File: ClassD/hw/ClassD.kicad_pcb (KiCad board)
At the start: 2 copper layers, 81.2 x 56.9 mm, 66 parts, among them P1 RedRCA, P2 WhiteRCA, P3 CONN_01X02, P4 CONN_01X02, P5 CONN_01X02, SW1 SW_PUSH, SW2 SW_PUSH, U1 TDA7491LP, U2 MCP1700T

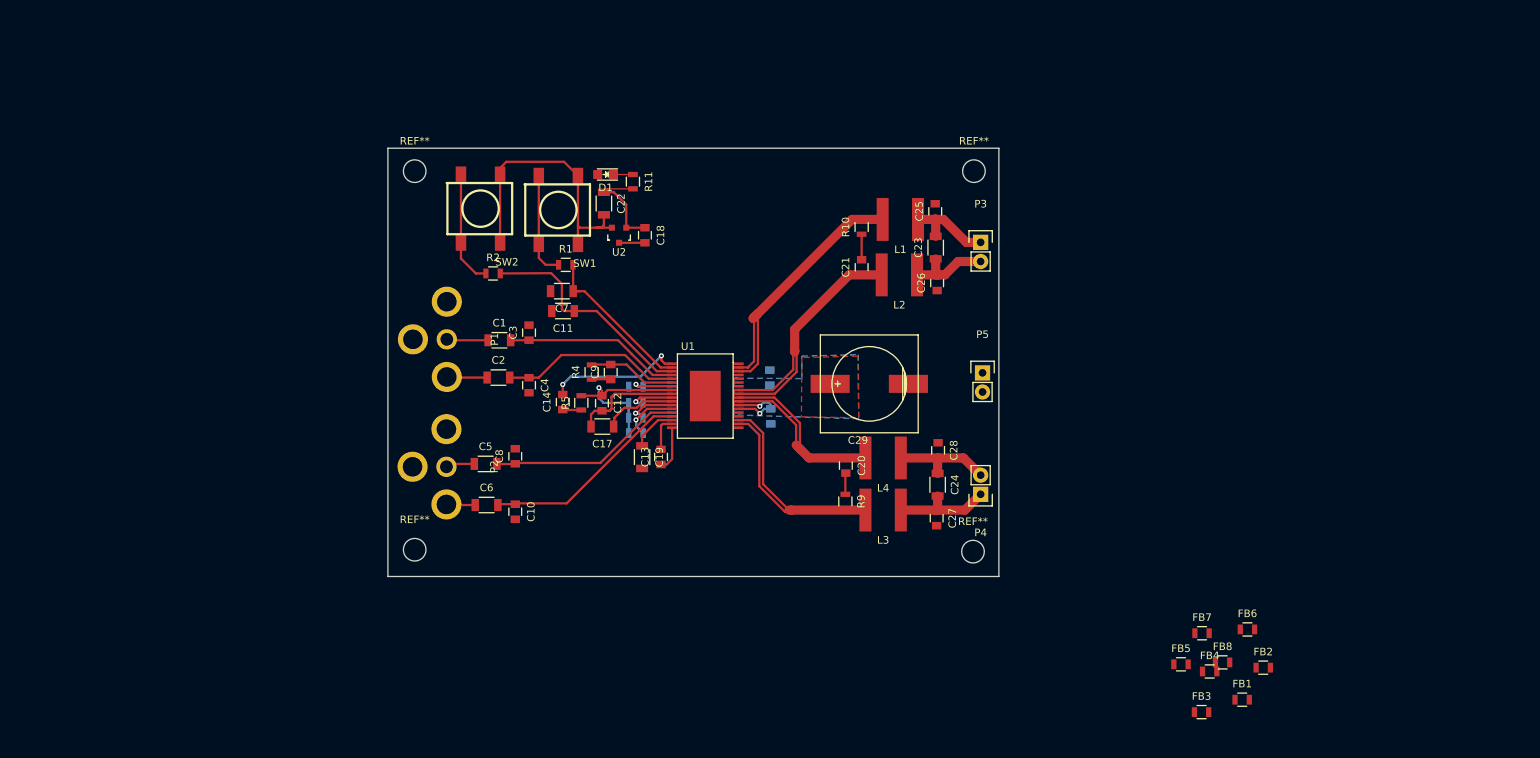
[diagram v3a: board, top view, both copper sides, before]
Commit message: Added planes and via stitching
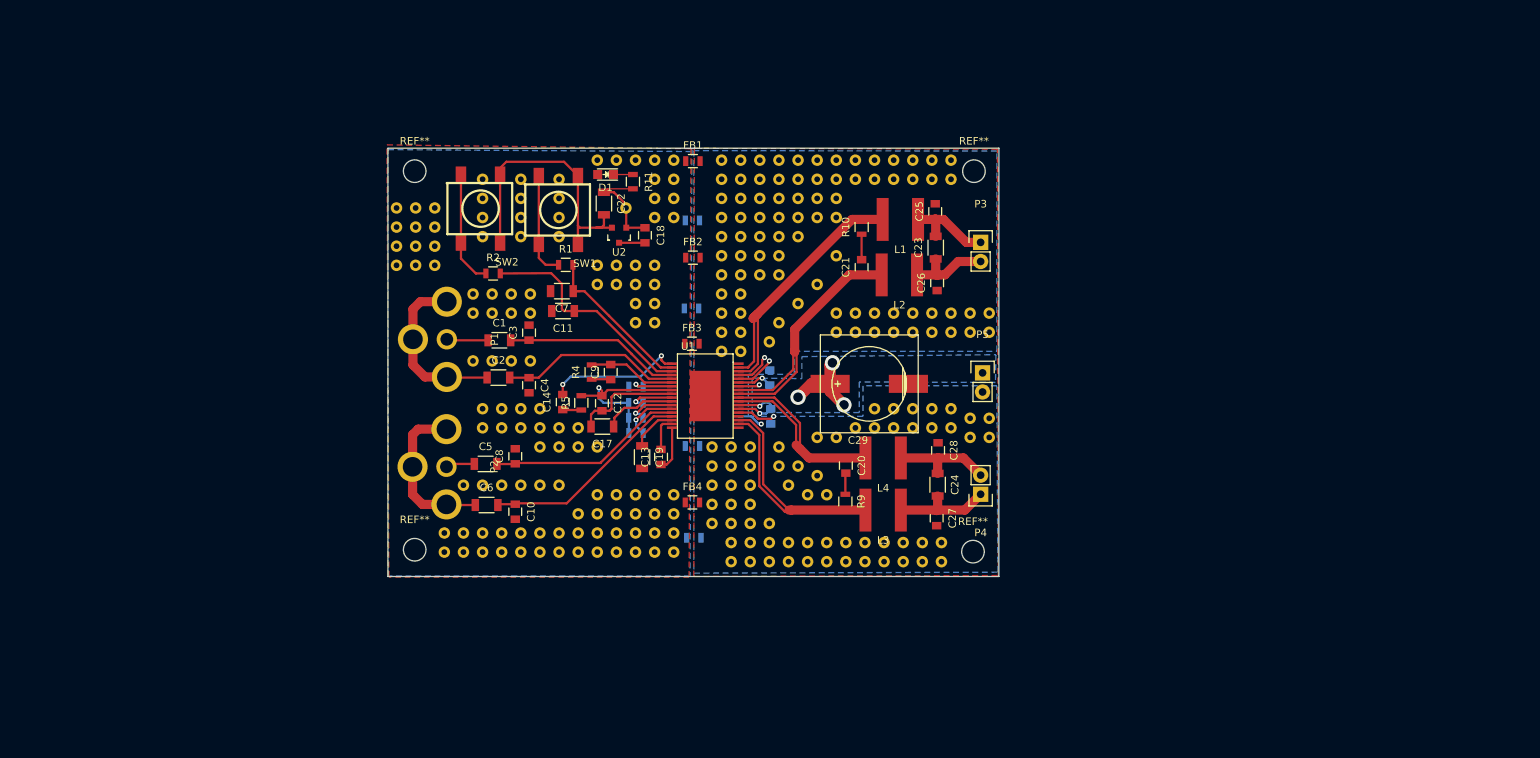
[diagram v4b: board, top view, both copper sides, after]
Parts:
- added REF**111111101: STITCH-VIA, ClassD:STITCH-VIA, F.Cu at (189.2, 88.9)
- added REF**111111102: STITCH-VIA, ClassD:STITCH-VIA, F.Cu at (189.2, 91.5)
- added REF**11111111: STITCH-VIA, ClassD:STITCH-VIA, F.Cu at (154.9, 110.5)
- added REF**11111111: STITCH-VIA, ClassD:STITCH-VIA, F.Cu at (149.8, 102.9)
- added REF**11111111: STITCH-VIA, ClassD:STITCH-VIA, F.Cu at (139.7, 94.0)
- added REF**11111111: STITCH-VIA, ClassD:STITCH-VIA, F.Cu at (139.7, 99.1)
- added REF**11111111: STITCH-VIA, ClassD:STITCH-VIA, F.Cu at (144.8, 96.5)
- added REF**11111111: STITCH-VIA, ClassD:STITCH-VIA, F.Cu at (144.8, 91.5)
- added REF**11111111: STITCH-VIA, ClassD:STITCH-VIA, F.Cu at (144.8, 94.0)
- added REF**11111111: STITCH-VIA, ClassD:STITCH-VIA, F.Cu at (144.8, 99.1)
- added REF**11111111: STITCH-VIA, ClassD:STITCH-VIA, F.Cu at (153.7, 95.3)
- added REF**11111111: STITCH-VIA, ClassD:STITCH-VIA, F.Cu at (157.5, 96.5)
- added REF**11111111: STITCH-VIA, ClassD:STITCH-VIA, F.Cu at (160.0, 96.5)
- added REF**11111111: STITCH-VIA, ClassD:STITCH-VIA, F.Cu at (157.5, 94.0)
- added REF**11111111: STITCH-VIA, ClassD:STITCH-VIA, F.Cu at (157.5, 105.4)
- added REF**11111111: STITCH-VIA, ClassD:STITCH-VIA, F.Cu at (160.0, 94.0)
- added REF**11111111: STITCH-VIA, ClassD:STITCH-VIA, F.Cu at (157.5, 91.5)
- added REF**11111111: STITCH-VIA, ClassD:STITCH-VIA, F.Cu at (160.0, 91.5)
- added REF**11111111: STITCH-VIA, ClassD:STITCH-VIA, F.Cu at (149.8, 88.9)
- added REF**11111111: STITCH-VIA, ClassD:STITCH-VIA, F.Cu at (152.4, 88.9)
- added REF**11111111: STITCH-VIA, ClassD:STITCH-VIA, F.Cu at (154.9, 88.9)
- added REF**11111111: STITCH-VIA, ClassD:STITCH-VIA, F.Cu at (157.5, 88.9)
- added REF**11111111: STITCH-VIA, ClassD:STITCH-VIA, F.Cu at (160.0, 88.9)
- added REF**11111111: STITCH-VIA, ClassD:STITCH-VIA, F.Cu at (166.4, 99.1)
- added REF**11111111: STITCH-VIA, ClassD:STITCH-VIA, F.Cu at (166.4, 88.9)
- added REF**11111111: STITCH-VIA, ClassD:STITCH-VIA, F.Cu at (157.5, 102.9)
- added REF**11111111: STITCH-VIA, ClassD:STITCH-VIA, F.Cu at (147.3, 124.5)
- added REF**11111111: STITCH-VIA, ClassD:STITCH-VIA, F.Cu at (144.8, 124.5)
- added REF**11111111: STITCH-VIA, ClassD:STITCH-VIA, F.Cu at (149.8, 127.0)
- added REF**11111111: STITCH-VIA, ClassD:STITCH-VIA, F.Cu at (147.3, 127.0)
- added REF**11111111: STITCH-VIA, ClassD:STITCH-VIA, F.Cu at (144.8, 127.0)
- added REF**11111111: STITCH-VIA, ClassD:STITCH-VIA, F.Cu at (142.2, 127.0)
- added REF**11111111: STITCH-VIA, ClassD:STITCH-VIA, F.Cu at (160.0, 141.0)
- added REF**11111111: STITCH-VIA, ClassD:STITCH-VIA, F.Cu at (157.5, 110.5)
- added REF**11111111: STITCH-VIA, ClassD:STITCH-VIA, F.Cu at (160.0, 138.4)
- added REF**11111111: STITCH-VIA, ClassD:STITCH-VIA, F.Cu at (160.0, 133.4)
- added REF**11111111: STITCH-VIA, ClassD:STITCH-VIA, F.Cu at (157.5, 133.4)
- added REF**11111111: STITCH-VIA, ClassD:STITCH-VIA, F.Cu at (154.9, 133.4)
- added REF**11111111: STITCH-VIA, ClassD:STITCH-VIA, F.Cu at (149.8, 133.4)
- added REF**11111111: STITCH-VIA, ClassD:STITCH-VIA, F.Cu at (152.4, 133.4)
- added REF**11111111: STITCH-VIA, ClassD:STITCH-VIA, F.Cu at (157.5, 135.9)
- added REF**11111111: STITCH-VIA, ClassD:STITCH-VIA, F.Cu at (154.9, 135.9)
- added REF**11111111: STITCH-VIA, ClassD:STITCH-VIA, F.Cu at (149.8, 135.9)
- added REF**11111111: STITCH-VIA, ClassD:STITCH-VIA, F.Cu at (152.4, 135.9)
- added REF**11111111: STITCH-VIA, ClassD:STITCH-VIA, F.Cu at (154.9, 108.0)
- added REF**11111111: STITCH-VIA, ClassD:STITCH-VIA, F.Cu at (160.0, 135.9)
- added REF**11111111: STITCH-VIA, ClassD:STITCH-VIA, F.Cu at (147.3, 135.9)
- added REF**11111111: STITCH-VIA, ClassD:STITCH-VIA, F.Cu at (154.9, 138.4)
- added REF**11111111: STITCH-VIA, ClassD:STITCH-VIA, F.Cu at (152.4, 138.4)
- added REF**11111111: STITCH-VIA, ClassD:STITCH-VIA, F.Cu at (147.3, 138.4)
- added REF**11111111: STITCH-VIA, ClassD:STITCH-VIA, F.Cu at (149.8, 138.4)
- added REF**11111111: STITCH-VIA, ClassD:STITCH-VIA, F.Cu at (157.5, 138.4)
- added REF**11111111: STITCH-VIA, ClassD:STITCH-VIA, F.Cu at (144.8, 138.4)
- added REF**11111111: STITCH-VIA, ClassD:STITCH-VIA, F.Cu at (154.9, 141.0)
- added REF**11111111: STITCH-VIA, ClassD:STITCH-VIA, F.Cu at (152.4, 141.0)
- added REF**11111111: STITCH-VIA, ClassD:STITCH-VIA, F.Cu at (157.5, 108.0)
- added REF**11111111: STITCH-VIA, ClassD:STITCH-VIA, F.Cu at (147.3, 141.0)
- added REF**11111111: STITCH-VIA, ClassD:STITCH-VIA, F.Cu at (149.8, 141.0)
- added REF**11111111: STITCH-VIA, ClassD:STITCH-VIA, F.Cu at (157.5, 141.0)
- added REF**11111111: STITCH-VIA, ClassD:STITCH-VIA, F.Cu at (144.8, 141.0)
- added REF**11111111: STITCH-VIA, ClassD:STITCH-VIA, F.Cu at (139.7, 141.0)
- added REF**11111111: STITCH-VIA, ClassD:STITCH-VIA, F.Cu at (137.1, 141.0)
- added REF**11111111: STITCH-VIA, ClassD:STITCH-VIA, F.Cu at (132.1, 141.0)
- added REF**11111111: STITCH-VIA, ClassD:STITCH-VIA, F.Cu at (134.6, 141.0)
- added REF**11111111: STITCH-VIA, ClassD:STITCH-VIA, F.Cu at (142.2, 141.0)
- added REF**11111111: STITCH-VIA, ClassD:STITCH-VIA, F.Cu at (129.5, 141.0)
- added REF**11111111: STITCH-VIA, ClassD:STITCH-VIA, F.Cu at (154.9, 102.9)
- added REF**11111111: STITCH-VIA, ClassD:STITCH-VIA, F.Cu at (139.7, 138.4)
- added REF**11111111: STITCH-VIA, ClassD:STITCH-VIA, F.Cu at (137.1, 138.4)
- added REF**11111111: STITCH-VIA, ClassD:STITCH-VIA, F.Cu at (132.1, 138.4)
- added REF**11111111: STITCH-VIA, ClassD:STITCH-VIA, F.Cu at (134.6, 138.4)
- added REF**11111111: STITCH-VIA, ClassD:STITCH-VIA, F.Cu at (142.2, 138.4)
- added REF**11111111: STITCH-VIA, ClassD:STITCH-VIA, F.Cu at (129.5, 138.4)
- added REF**11111111: STITCH-VIA, ClassD:STITCH-VIA, F.Cu at (142.2, 132.1)
- added REF**11111111: STITCH-VIA, ClassD:STITCH-VIA, F.Cu at (144.8, 132.1)
- added REF**11111111: STITCH-VIA, ClassD:STITCH-VIA, F.Cu at (132.1, 132.1)
- added REF**11111111: STITCH-VIA, ClassD:STITCH-VIA, F.Cu at (134.6, 132.1)
- added REF**11111111: STITCH-VIA, ClassD:STITCH-VIA, F.Cu at (152.4, 105.4)
- added REF**11111111: STITCH-VIA, ClassD:STITCH-VIA, F.Cu at (137.1, 132.1)
- added REF**11111111: STITCH-VIA, ClassD:STITCH-VIA, F.Cu at (139.7, 132.1)
- added REF**11111111: STITCH-VIA, ClassD:STITCH-VIA, F.Cu at (134.6, 124.5)
- added REF**11111111: STITCH-VIA, ClassD:STITCH-VIA, F.Cu at (137.1, 124.5)
- added REF**11111111: STITCH-VIA, ClassD:STITCH-VIA, F.Cu at (139.7, 124.5)
- added REF**11111111: STITCH-VIA, ClassD:STITCH-VIA, F.Cu at (142.2, 124.5)
- added REF**11111111: STITCH-VIA, ClassD:STITCH-VIA, F.Cu at (134.6, 121.9)
- added REF**11111111: STITCH-VIA, ClassD:STITCH-VIA, F.Cu at (137.1, 121.9)
- added REF**11111111: STITCH-VIA, ClassD:STITCH-VIA, F.Cu at (139.7, 121.9)
- added REF**11111111: STITCH-VIA, ClassD:STITCH-VIA, F.Cu at (142.2, 121.9)
- added REF**11111111: STITCH-VIA, ClassD:STITCH-VIA, F.Cu at (154.9, 105.4)
- added REF**11111111: STITCH-VIA, ClassD:STITCH-VIA, F.Cu at (133.3, 115.6)
- added REF**11111111: STITCH-VIA, ClassD:STITCH-VIA, F.Cu at (135.9, 115.6)
- added REF**11111111: STITCH-VIA, ClassD:STITCH-VIA, F.Cu at (138.4, 115.6)
- added REF**11111111: STITCH-VIA, ClassD:STITCH-VIA, F.Cu at (141.0, 115.6)
- added REF**11111111: STITCH-VIA, ClassD:STITCH-VIA, F.Cu at (133.3, 109.2)
- added REF**11111111: STITCH-VIA, ClassD:STITCH-VIA, F.Cu at (135.9, 109.2)
- added REF**11111111: STITCH-VIA, ClassD:STITCH-VIA, F.Cu at (138.4, 109.2)
- added REF**11111111: STITCH-VIA, ClassD:STITCH-VIA, F.Cu at (141.0, 109.2)
- added REF**11111111: STITCH-VIA, ClassD:STITCH-VIA, F.Cu at (141.0, 106.7)
- added REF**11111111: STITCH-VIA, ClassD:STITCH-VIA, F.Cu at (138.4, 106.7)
- added REF**11111111: STITCH-VIA, ClassD:STITCH-VIA, F.Cu at (149.8, 105.4)
- added REF**11111111: STITCH-VIA, ClassD:STITCH-VIA, F.Cu at (133.3, 106.7)
- added REF**11111111: STITCH-VIA, ClassD:STITCH-VIA, F.Cu at (135.9, 106.7)
- added REF**11111111: STITCH-VIA, ClassD:STITCH-VIA, F.Cu at (128.3, 100.3)
- added REF**11111111: STITCH-VIA, ClassD:STITCH-VIA, F.Cu at (128.3, 95.3)
- added REF**11111111: STITCH-VIA, ClassD:STITCH-VIA, F.Cu at (128.3, 97.8)
- added REF**11111111: STITCH-VIA, ClassD:STITCH-VIA, F.Cu at (128.3, 102.9)
- added REF**11111111: STITCH-VIA, ClassD:STITCH-VIA, F.Cu at (125.7, 100.3)
- added REF**11111111: STITCH-VIA, ClassD:STITCH-VIA, F.Cu at (125.7, 95.3)
- added REF**11111111: STITCH-VIA, ClassD:STITCH-VIA, F.Cu at (125.7, 97.8)
- added REF**11111111: STITCH-VIA, ClassD:STITCH-VIA, F.Cu at (125.7, 102.9)
- added REF**11111111: STITCH-VIA, ClassD:STITCH-VIA, F.Cu at (152.4, 102.9)
- added REF**11111111: STITCH-VIA, ClassD:STITCH-VIA, F.Cu at (123.2, 100.3)
- added REF**11111111: STITCH-VIA, ClassD:STITCH-VIA, F.Cu at (123.2, 95.3)
- added REF**11111111: STITCH-VIA, ClassD:STITCH-VIA, F.Cu at (123.2, 97.8)
- added REF**11111111: STITCH-VIA, ClassD:STITCH-VIA, F.Cu at (123.2, 102.9)
- added REF**11111111: STITCH-VIA, ClassD:STITCH-VIA, F.Cu at (134.6, 96.5)
- added REF**11111111: STITCH-VIA, ClassD:STITCH-VIA, F.Cu at (134.6, 91.5)
- added REF**11111111: STITCH-VIA, ClassD:STITCH-VIA, F.Cu at (134.6, 94.0)
- added REF**11111111: STITCH-VIA, ClassD:STITCH-VIA, F.Cu at (134.6, 99.1)
- added REF**11111111: STITCH-VIA, ClassD:STITCH-VIA, F.Cu at (139.7, 96.5)
- added REF**11111111: STITCH-VIA, ClassD:STITCH-VIA, F.Cu at (139.7, 91.5)
- added REF**111111111: STITCH-VIA, ClassD:STITCH-VIA, F.Cu at (196.8, 111.8)
- added REF**111111111: STITCH-VIA, ClassD:STITCH-VIA, F.Cu at (191.8, 111.8)
- added REF**111111111: STITCH-VIA, ClassD:STITCH-VIA, F.Cu at (186.7, 111.8)
- added REF**111111111: STITCH-VIA, ClassD:STITCH-VIA, F.Cu at (181.6, 111.8)
- added REF**111111111: STITCH-VIA, ClassD:STITCH-VIA, F.Cu at (166.4, 114.3)
- added REF**111111111: STITCH-VIA, ClassD:STITCH-VIA, F.Cu at (166.4, 109.2)
- added REF**111111111: STITCH-VIA, ClassD:STITCH-VIA, F.Cu at (166.4, 104.2)
- added REF**111111111: STITCH-VIA, ClassD:STITCH-VIA, F.Cu at (166.4, 94.0)
- added REF**111111111: STITCH-VIA, ClassD:STITCH-VIA, F.Cu at (191.8, 88.9)
- added REF**111111112: STITCH-VIA, ClassD:STITCH-VIA, F.Cu at (166.4, 96.5)
- added REF**111111112: STITCH-VIA, ClassD:STITCH-VIA, F.Cu at (191.8, 91.5)
- added REF**11111112: STITCH-VIA, ClassD:STITCH-VIA, F.Cu at (196.8, 109.2)
- added REF**11111112: STITCH-VIA, ClassD:STITCH-VIA, F.Cu at (191.8, 109.2)
- added REF**11111112: STITCH-VIA, ClassD:STITCH-VIA, F.Cu at (186.7, 109.2)
- added REF**11111112: STITCH-VIA, ClassD:STITCH-VIA, F.Cu at (181.6, 109.2)
- added REF**11111112: STITCH-VIA, ClassD:STITCH-VIA, F.Cu at (166.4, 111.8)
- added REF**11111112: STITCH-VIA, ClassD:STITCH-VIA, F.Cu at (166.4, 106.7)
- added REF**11111112: STITCH-VIA, ClassD:STITCH-VIA, F.Cu at (166.4, 101.6)
- added REF**11111112: STITCH-VIA, ClassD:STITCH-VIA, F.Cu at (166.4, 91.5)
- added REF**111111121: STITCH-VIA, ClassD:STITCH-VIA, F.Cu at (170.2, 142.3)
- added REF**111111121: STITCH-VIA, ClassD:STITCH-VIA, F.Cu at (193.0, 142.3)
- added REF**111111121: STITCH-VIA, ClassD:STITCH-VIA, F.Cu at (195.6, 142.3)
- added REF**111111121: STITCH-VIA, ClassD:STITCH-VIA, F.Cu at (187.9, 142.3)
- added REF**111111121: STITCH-VIA, ClassD:STITCH-VIA, F.Cu at (181.6, 101.6)
- added REF**111111121: STITCH-VIA, ClassD:STITCH-VIA, F.Cu at (179.1, 105.4)
- added REF**111111121: STITCH-VIA, ClassD:STITCH-VIA, F.Cu at (176.5, 108.0)
- added REF**111111121: STITCH-VIA, ClassD:STITCH-VIA, F.Cu at (174.0, 110.5)
- added REF**111111121: STITCH-VIA, ClassD:STITCH-VIA, F.Cu at (172.7, 113.0)
- added REF**111111121: STITCH-VIA, ClassD:STITCH-VIA, F.Cu at (179.1, 125.7)
- added REF**111111121: STITCH-VIA, ClassD:STITCH-VIA, F.Cu at (181.6, 125.7)
- added REF**111111121: STITCH-VIA, ClassD:STITCH-VIA, F.Cu at (172.7, 142.3)
- added REF**111111121: STITCH-VIA, ClassD:STITCH-VIA, F.Cu at (176.5, 129.6)
- added REF**111111121: STITCH-VIA, ClassD:STITCH-VIA, F.Cu at (177.8, 133.4)
- added REF**111111121: STITCH-VIA, ClassD:STITCH-VIA, F.Cu at (180.3, 133.4)
- added REF**111111121: STITCH-VIA, ClassD:STITCH-VIA, F.Cu at (179.1, 130.8)
- added REF**111111121: STITCH-VIA, ClassD:STITCH-VIA, F.Cu at (175.2, 132.1)
- added REF**111111121: STITCH-VIA, ClassD:STITCH-VIA, F.Cu at (174.0, 129.6)
- added REF**111111121: STITCH-VIA, ClassD:STITCH-VIA, F.Cu at (174.0, 127.0)
- added REF**111111121: STITCH-VIA, ClassD:STITCH-VIA, F.Cu at (184.1, 124.5)
- added REF**111111121: STITCH-VIA, ClassD:STITCH-VIA, F.Cu at (186.7, 124.5)
- added REF**111111121: STITCH-VIA, ClassD:STITCH-VIA, F.Cu at (189.2, 124.5)
- added REF**111111121: STITCH-VIA, ClassD:STITCH-VIA, F.Cu at (175.2, 142.3)
- added REF**111111121: STITCH-VIA, ClassD:STITCH-VIA, F.Cu at (191.8, 124.5)
- added REF**111111121: STITCH-VIA, ClassD:STITCH-VIA, F.Cu at (194.3, 124.5)
- added REF**111111121: STITCH-VIA, ClassD:STITCH-VIA, F.Cu at (196.8, 124.5)
- added REF**111111121: STITCH-VIA, ClassD:STITCH-VIA, F.Cu at (199.4, 125.7)
- added REF**111111121: STITCH-VIA, ClassD:STITCH-VIA, F.Cu at (201.9, 125.7)
- added REF**111111121: STITCH-VIA, ClassD:STITCH-VIA, F.Cu at (201.9, 111.8)
- added REF**111111121: STITCH-VIA, ClassD:STITCH-VIA, F.Cu at (199.4, 111.8)
- added REF**111111121: STITCH-VIA, ClassD:STITCH-VIA, F.Cu at (194.3, 111.8)
- added REF**111111121: STITCH-VIA, ClassD:STITCH-VIA, F.Cu at (189.2, 111.8)
- added REF**111111121: STITCH-VIA, ClassD:STITCH-VIA, F.Cu at (184.1, 111.8)
- added REF**111111121: STITCH-VIA, ClassD:STITCH-VIA, F.Cu at (167.6, 142.3)
- added REF**111111121: STITCH-VIA, ClassD:STITCH-VIA, F.Cu at (168.9, 114.3)
- added REF**111111121: STITCH-VIA, ClassD:STITCH-VIA, F.Cu at (168.9, 109.2)
- added REF**111111121: STITCH-VIA, ClassD:STITCH-VIA, F.Cu at (168.9, 104.2)
- added REF**111111121: STITCH-VIA, ClassD:STITCH-VIA, F.Cu at (168.9, 94.0)
- added REF**111111121: STITCH-VIA, ClassD:STITCH-VIA, F.Cu at (194.3, 88.9)
- added REF**111111121: STITCH-VIA, ClassD:STITCH-VIA, F.Cu at (180.3, 142.3)
- added REF**111111121: STITCH-VIA, ClassD:STITCH-VIA, F.Cu at (182.9, 142.3)
- added REF**111111121: STITCH-VIA, ClassD:STITCH-VIA, F.Cu at (185.4, 142.3)
- added REF**111111121: STITCH-VIA, ClassD:STITCH-VIA, F.Cu at (177.8, 142.3)
- added REF**111111121: STITCH-VIA, ClassD:STITCH-VIA, F.Cu at (190.5, 142.3)
- added REF**111111122: STITCH-VIA, ClassD:STITCH-VIA, F.Cu at (168.9, 96.5)
- added REF**111111122: STITCH-VIA, ClassD:STITCH-VIA, F.Cu at (194.3, 91.5)
- added REF**111111131: STITCH-VIA, ClassD:STITCH-VIA, F.Cu at (171.4, 104.2)
- added REF**111111131: STITCH-VIA, ClassD:STITCH-VIA, F.Cu at (171.4, 94.0)
- added REF**111111131: STITCH-VIA, ClassD:STITCH-VIA, F.Cu at (196.8, 88.9)
- added REF**111111132: STITCH-VIA, ClassD:STITCH-VIA, F.Cu at (171.4, 96.5)
- added REF**111111132: STITCH-VIA, ClassD:STITCH-VIA, F.Cu at (196.8, 91.5)
- added REF**111111141: STITCH-VIA, ClassD:STITCH-VIA, F.Cu at (174.0, 104.2)
- added REF**111111141: STITCH-VIA, ClassD:STITCH-VIA, F.Cu at (174.0, 94.0)
- added REF**111111142: STITCH-VIA, ClassD:STITCH-VIA, F.Cu at (174.0, 96.5)
- added REF**111111151: STITCH-VIA, ClassD:STITCH-VIA, F.Cu at (176.5, 94.0)
- added REF**111111152: STITCH-VIA, ClassD:STITCH-VIA, F.Cu at (176.5, 99.1)
- added REF**111111152: STITCH-VIA, ClassD:STITCH-VIA, F.Cu at (176.5, 96.5)
- added REF**111111161: STITCH-VIA, ClassD:STITCH-VIA, F.Cu at (179.1, 94.0)
- added REF**111111162: STITCH-VIA, ClassD:STITCH-VIA, F.Cu at (179.1, 96.5)
- added REF**111111171: STITCH-VIA, ClassD:STITCH-VIA, F.Cu at (181.6, 94.0)
- added REF**111111172: STITCH-VIA, ClassD:STITCH-VIA, F.Cu at (181.6, 96.5)
- added REF**11111121: STITCH-VIA, ClassD:STITCH-VIA, F.Cu at (168.9, 99.1)
- added REF**11111121: STITCH-VIA, ClassD:STITCH-VIA, F.Cu at (168.9, 88.9)
- added REF**11111122: STITCH-VIA, ClassD:STITCH-VIA, F.Cu at (170.2, 127.0)
- added REF**11111122: STITCH-VIA, ClassD:STITCH-VIA, F.Cu at (170.2, 134.6)
- added REF**11111122: STITCH-VIA, ClassD:STITCH-VIA, F.Cu at (165.1, 134.6)
- added REF**11111122: STITCH-VIA, ClassD:STITCH-VIA, F.Cu at (167.6, 134.6)
- added REF**11111122: STITCH-VIA, ClassD:STITCH-VIA, F.Cu at (172.7, 137.2)
- added REF**11111122: STITCH-VIA, ClassD:STITCH-VIA, F.Cu at (170.2, 137.2)
- added REF**11111122: STITCH-VIA, ClassD:STITCH-VIA, F.Cu at (165.1, 137.2)
- added REF**11111122: STITCH-VIA, ClassD:STITCH-VIA, F.Cu at (167.6, 137.2)
- added REF**11111122: STITCH-VIA, ClassD:STITCH-VIA, F.Cu at (170.2, 139.7)
- added REF**11111122: STITCH-VIA, ClassD:STITCH-VIA, F.Cu at (167.6, 139.7)
- added REF**11111122: STITCH-VIA, ClassD:STITCH-VIA, F.Cu at (172.7, 139.7)
- added REF**11111122: STITCH-VIA, ClassD:STITCH-VIA, F.Cu at (167.6, 127.0)
- added REF**11111122: STITCH-VIA, ClassD:STITCH-VIA, F.Cu at (175.2, 139.7)
- added REF**11111122: STITCH-VIA, ClassD:STITCH-VIA, F.Cu at (180.3, 139.7)
- added REF**11111122: STITCH-VIA, ClassD:STITCH-VIA, F.Cu at (177.8, 139.7)
- added REF**11111122: STITCH-VIA, ClassD:STITCH-VIA, F.Cu at (182.9, 139.7)
- added REF**11111122: STITCH-VIA, ClassD:STITCH-VIA, F.Cu at (185.4, 139.7)
- added REF**11111122: STITCH-VIA, ClassD:STITCH-VIA, F.Cu at (190.5, 139.7)
- added REF**11111122: STITCH-VIA, ClassD:STITCH-VIA, F.Cu at (187.9, 139.7)
- added REF**11111122: STITCH-VIA, ClassD:STITCH-VIA, F.Cu at (193.0, 139.7)
- added REF**11111122: STITCH-VIA, ClassD:STITCH-VIA, F.Cu at (195.6, 139.7)
- added REF**11111122: STITCH-VIA, ClassD:STITCH-VIA, F.Cu at (186.7, 121.9)
- added REF**11111122: STITCH-VIA, ClassD:STITCH-VIA, F.Cu at (165.1, 127.0)
- added REF**11111122: STITCH-VIA, ClassD:STITCH-VIA, F.Cu at (189.2, 121.9)
- added REF**11111122: STITCH-VIA, ClassD:STITCH-VIA, F.Cu at (191.8, 121.9)
- added REF**11111122: STITCH-VIA, ClassD:STITCH-VIA, F.Cu at (194.3, 121.9)
- added REF**11111122: STITCH-VIA, ClassD:STITCH-VIA, F.Cu at (196.8, 121.9)
- added REF**11111122: STITCH-VIA, ClassD:STITCH-VIA, F.Cu at (199.4, 123.2)
- added REF**11111122: STITCH-VIA, ClassD:STITCH-VIA, F.Cu at (201.9, 123.2)
- added REF**11111122: STITCH-VIA, ClassD:STITCH-VIA, F.Cu at (201.9, 109.2)
- added REF**11111122: STITCH-VIA, ClassD:STITCH-VIA, F.Cu at (199.4, 109.2)
- added REF**11111122: STITCH-VIA, ClassD:STITCH-VIA, F.Cu at (194.3, 109.2)
- added REF**11111122: STITCH-VIA, ClassD:STITCH-VIA, F.Cu at (189.2, 109.2)
- added REF**11111122: STITCH-VIA, ClassD:STITCH-VIA, F.Cu at (170.2, 129.6)
- added REF**11111122: STITCH-VIA, ClassD:STITCH-VIA, F.Cu at (184.1, 109.2)
- added REF**11111122: STITCH-VIA, ClassD:STITCH-VIA, F.Cu at (168.9, 111.8)
- added REF**11111122: STITCH-VIA, ClassD:STITCH-VIA, F.Cu at (168.9, 106.7)
- added REF**11111122: STITCH-VIA, ClassD:STITCH-VIA, F.Cu at (168.9, 101.6)
- added REF**11111122: STITCH-VIA, ClassD:STITCH-VIA, F.Cu at (168.9, 91.5)
- added REF**11111122: STITCH-VIA, ClassD:STITCH-VIA, F.Cu at (165.1, 129.6)
- added REF**11111122: STITCH-VIA, ClassD:STITCH-VIA, F.Cu at (167.6, 129.6)
- added REF**11111122: STITCH-VIA, ClassD:STITCH-VIA, F.Cu at (170.2, 132.1)
- added REF**11111122: STITCH-VIA, ClassD:STITCH-VIA, F.Cu at (165.1, 132.1)
- added REF**11111122: STITCH-VIA, ClassD:STITCH-VIA, F.Cu at (167.6, 132.1)
- added REF**11111131: STITCH-VIA, ClassD:STITCH-VIA, F.Cu at (171.4, 99.1)
- added REF**11111131: STITCH-VIA, ClassD:STITCH-VIA, F.Cu at (171.4, 88.9)
- added REF**11111132: STITCH-VIA, ClassD:STITCH-VIA, F.Cu at (171.4, 101.6)
- added REF**11111132: STITCH-VIA, ClassD:STITCH-VIA, F.Cu at (171.4, 91.5)
- added REF**11111141: STITCH-VIA, ClassD:STITCH-VIA, F.Cu at (174.0, 99.1)
- added REF**11111141: STITCH-VIA, ClassD:STITCH-VIA, F.Cu at (174.0, 88.9)
- added REF**11111142: STITCH-VIA, ClassD:STITCH-VIA, F.Cu at (174.0, 101.6)
- added REF**11111142: STITCH-VIA, ClassD:STITCH-VIA, F.Cu at (174.0, 91.5)
- added REF**11111151: STITCH-VIA, ClassD:STITCH-VIA, F.Cu at (176.5, 88.9)
- added REF**11111152: STITCH-VIA, ClassD:STITCH-VIA, F.Cu at (176.5, 91.5)
- added REF**11111161: STITCH-VIA, ClassD:STITCH-VIA, F.Cu at (179.1, 88.9)
- added REF**11111162: STITCH-VIA, ClassD:STITCH-VIA, F.Cu at (179.1, 91.5)
- added REF**11111171: STITCH-VIA, ClassD:STITCH-VIA, F.Cu at (181.6, 88.9)
- added REF**11111172: STITCH-VIA, ClassD:STITCH-VIA, F.Cu at (181.6, 91.5)
- added REF**11111181: STITCH-VIA, ClassD:STITCH-VIA, F.Cu at (184.1, 88.9)
- added REF**11111182: STITCH-VIA, ClassD:STITCH-VIA, F.Cu at (184.1, 91.5)
- added REF**11111191: STITCH-VIA, ClassD:STITCH-VIA, F.Cu at (186.7, 88.9)
- added REF**11111192: STITCH-VIA, ClassD:STITCH-VIA, F.Cu at (186.7, 91.5)
- FB5, FB6, FB7, FB8: moved to B.Cu
- moved FB1 102.2 mm to (162.5, 89.0)
- moved FB2 93.3 mm to (162.5, 101.9)
- moved FB8 91.7 mm to (162.5, 96.9)
- moved FB3 83.5 mm to (162.4, 113.3)
- moved FB7 80.4 mm to (162.4, 108.6)
- moved FB6 77.7 mm to (162.5, 126.9)
- moved FB4 72.3 mm to (162.5, 134.4)
- moved FB5 66.9 mm to (162.7, 139.1)
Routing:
- net Net-(C6-Pad1): track 3.87 -> 21.7 mm
- net Net-(C2-Pad1): track 5.39 -> 22.9 mm
- net OGND: track 0.00 -> 16.3 mm, vias 0 -> 3
- net Net-(C21-Pad1): track 28.1 -> 40.7 mm
- net /VCC: track 26.1 -> 33.0 mm, vias 2 -> 7
- net (no net): track 0.00 -> 3.47 mm, vias 0 -> 1
- added copper zone on B.Cu, net GND
- added copper zone on F.Cu, net GND
- added copper zone on B.Cu, net OGND
- added copper zone on F.Cu, net OGND
- removed copper zone on F.Cu, net /VCC
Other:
- rule pad_to_mask_clearance: 0.2 -> 0.0762
